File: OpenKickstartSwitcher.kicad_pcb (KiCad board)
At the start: 2 copper layers, 28.4 x 76.5 mm, 14 parts, among them J1 Conn_01x03, J2 Conn_01x04, J4 Conn_01x03, J98 LOGO, J99 OSHW_LOGO, U1 KS_SOCKET, U2 M27C800, U3 7400

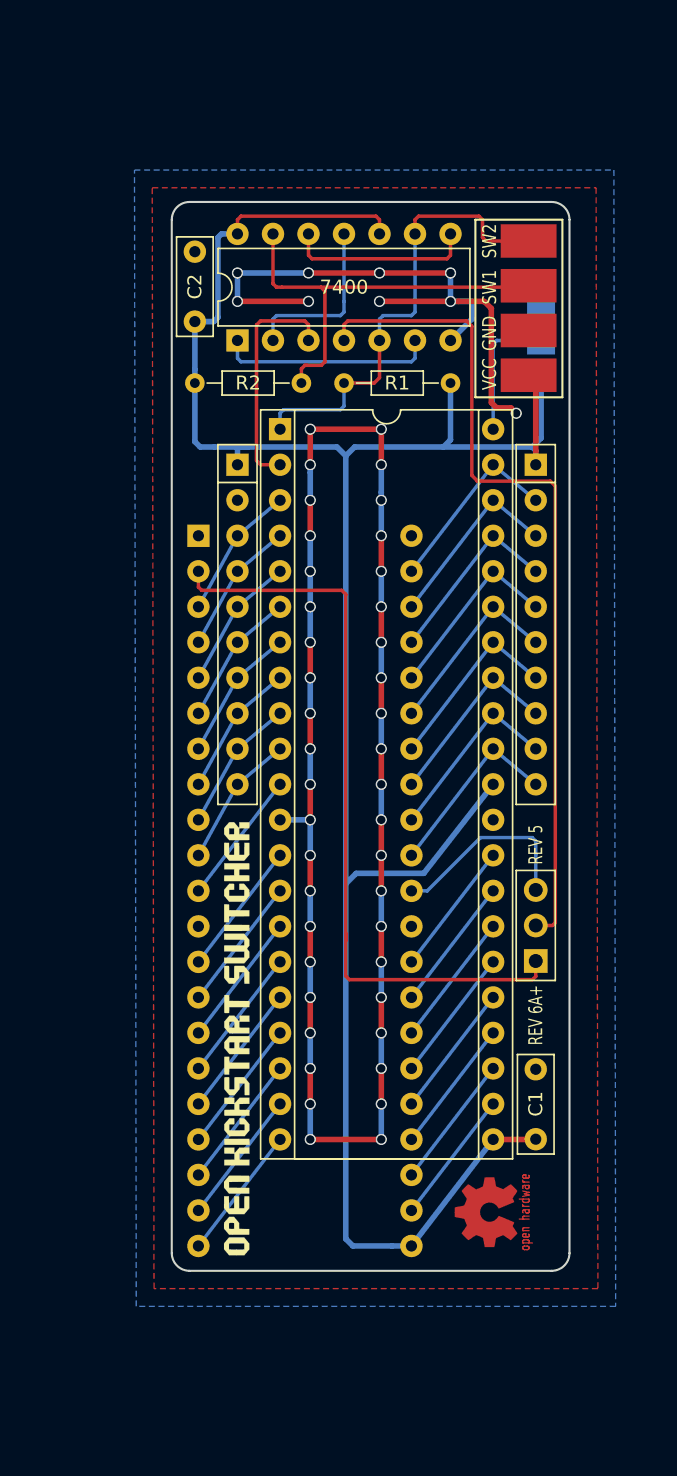
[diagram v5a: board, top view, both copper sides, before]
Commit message: Initial commit of CDTV version - NOT READY YET
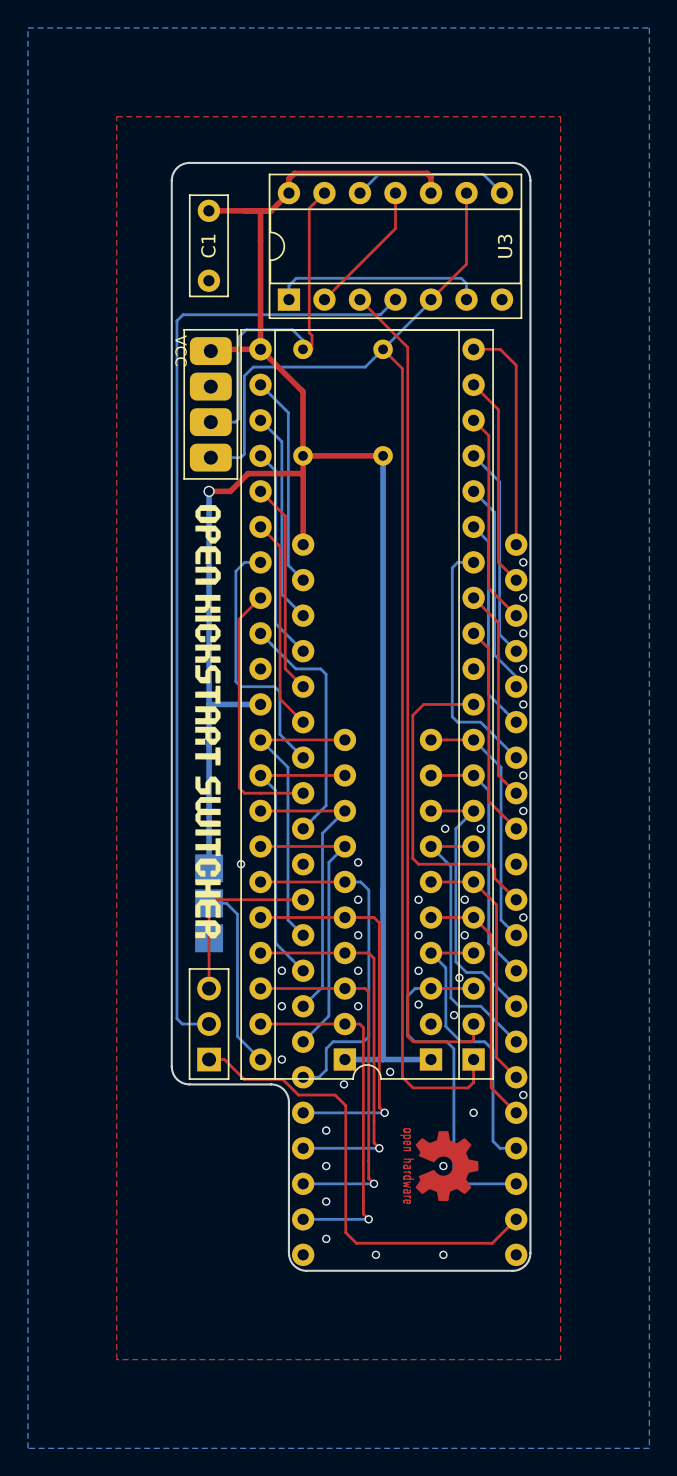
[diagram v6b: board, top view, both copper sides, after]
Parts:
- removed C2: 100n, Capacitors_THT:C_Disc_D7.0mm_W2.5mm_P5.00mm
- C1: footprint Capacitors_THT:C_Disc_D7.0mm_W2.5mm_P5.00mm -> Capacitor_THT:C_Disc_D7.0mm_W2.5mm_P5.00mm
- J2: footprint OpenKickstartSwitcher:LoosePads-4 -> OpenKickstartSwitcher:Solderable_PinHeader_1x04
- R1, R2: footprint Resistors_THT:R_Axial_DIN0204_L3.6mm_D1.6mm_P7.62mm_Horizontal -> Resistor_THT:R_Axial_DIN0204_L3.6mm_D1.6mm_P7.62mm_Horizontal; moved to B.Cu
- RN1, RN2: footprint Resistors_THT:R_Array_SIP10 -> Resistor_THT:R_Array_SIP10; moved to B.Cu
- U3: footprint Housings_DIP:DIP-14_W7.62mm -> Package_DIP:DIP-14_W7.62mm_Socket
- moved C1 70.4 mm to (146.3, 89.3), turned to 270 degrees
- moved U1 56.2 mm to (168.3, 164.0), turned to 180 degrees
- moved U2 47.2 mm to (165.2, 150.0), turned to 180 degrees
- moved J4 46.7 mm to (146.3, 138.8), turned to 270 degrees
- moved RN1 44.7 mm to (162.2, 150.0), turned to 90 degrees
- moved RN2 44.7 mm to (156.0, 150.0), turned to 90 degrees
- moved J2 25.1 mm to (146.4, 106.9), turned to 180 degrees
- moved J1 24.4 mm to (146.3, 150.0)
- moved J98 22.7 mm to (146.2, 125.9), turned to 270 degrees
- moved R2 9.32 mm to (153.0, 106.8), turned to 90 degrees
- moved R1 7.10 mm to (158.8, 106.8), turned to 90 degrees
- moved U3 4.70 mm to (152.0, 95.6)
- moved J99 4.33 mm to (163.3, 157.6), turned to 270 degrees
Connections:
- U1 pad 1: (no net) -> Net-(U1-Pad1)
- U1 pad 42: (no net) -> Net-(U1-Pad42)
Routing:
- net GND: track 160.3 -> 0.00 mm, vias 51 -> 38
- net /sw18: track 33.5 -> 92.4 mm
- net Net-(U2-Pad2): track 16.6 -> 60.2 mm
- net Net-(J1-Pad1): track 54.6 -> 33.4 mm
- net VCC: track 162.9 -> 144.1 mm, vias 0 -> 1
- net /a7: track 9.77 -> 25.1 mm
- net /a11: track 13.6 -> 28.2 mm, vias 0 -> 1
- net Net-(U1-Pad11): track 9.60 -> 23.9 mm
- net /a10: track 13.6 -> 27.5 mm, vias 0 -> 1
- net /a9: track 13.6 -> 26.8 mm, vias 0 -> 1
- net /a8: track 13.6 -> 26.0 mm, vias 0 -> 1
- net /a12: track 13.6 -> 25.3 mm
- net /a6: track 9.77 -> 21.2 mm
- net /a3: track 9.77 -> 20.4 mm
- net /a2: track 9.77 -> 20.0 mm
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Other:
- board size 28.4 x 76.5 mm -> 25.7 x 79.2 mm
- net class Default: clearance 0.25 -> 0.16; trace_width 0.25 -> 0.2
- net class Power: clearance 0.25 -> 0.16
- rule trace_clearance: 0.25 -> 0.16
- board text removed: "A19"
- board text removed: "GND"
- board text removed: "REV 5"
- board text removed: "REV 6A+"
- board text removed: "SW1"
- board text removed: "SW2"
- board text removed: "V2"
- board text removed: "github.com/SukkoPera/OpenKickstartSwitcher"

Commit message: Work in progress
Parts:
- moved C1 0.27 mm to (146.6, 89.3)
- moved J2 0.25 mm to (146.7, 106.9)
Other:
- board text added: "GND"
- board text added: "SW1"
- board text added: "SW2"
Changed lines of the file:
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@@
   (general
     (thickness 1.6)
-    (drawings 19)
+    (drawings 22)
     (tracks 347)
     (zones 0)
@@
   )
   (module OpenKickstartSwitcher:Solderable_PinHeader_1x04 (layer F.Cu)
-    (at 146.431 106.934 180)
+    (at 146.685 106.934 180)
     (descr "Through hole straight pin header, 1x04, 2.54mm pitch, single row")
     (tags "Through hole pin header THT 1x04 2.54mm single row")
@@
     (fp_line (start -1.27 8.89) (end -1.27 -0.635) (layer F.Fab) (width 0.1))
     (fp_line (start -1.27 -0.635) (end -0.635 -1.27) (layer F.Fab) (width 0.1))
-    (fp_line (start -1.905 9.144) (end 1.905 9.144) (layer F.SilkS) (width 0.12))
-    (fp_line (start -1.905 -1.524) (end -1.905 9.144) (layer F.SilkS) (width 0.12))
-    (fp_line (start 1.905 -1.524) (end 1.905 9.144) (layer F.SilkS) (width 0.12))
-    (fp_line (start -1.905 -1.524) (end 1.905 -1.524) (layer F.SilkS) (width 0.12))
     (fp_line (start -1.8 -1.8) (end -1.8 9.4) (layer F.CrtYd) (width 0.05))
     (fp_line (start -1.8 9.4) (end 1.8 9.4) (layer F.CrtYd) (width 0.05))
@@
       (effects (font (size 1 1) (thickness 0.15)))
     )
-    (pad 1 thru_hole roundrect (at 0 0 180) (size 3 2) (drill 1) (layers *.Cu *.Mask) (roundrect_rratio 0.25)
+    (pad 1 thru_hole roundrect (at 0 0 180) (size 2.8 2) (drill 1) (layers *.Cu *.Mask) (roundrect_rratio 0.25)
       (net 3 /sw18))
-    (pad 2 thru_hole roundrect (at 0 2.54 180) (size 3 2) (drill 1) (layers *.Cu *.Mask) (roundrect_rratio 0.25)
+    (pad 2 thru_hole roundrect (at 0 2.54 180) (size 2.8 2) (drill 1) (layers *.Cu *.Mask) (roundrect_rratio 0.25)
       (net 4 /sw17))
-    (pad 3 thru_hole roundrect (at 0 5.08 180) (size 3 2) (drill 1) (layers *.Cu *.Mask) (roundrect_rratio 0.25)
+    (pad 3 thru_hole roundrect (at 0 5.08 180) (size 2.8 2) (drill 1) (layers *.Cu *.Mask) (roundrect_rratio 0.25)
       (net 5 GND))
-    (pad 4 thru_hole roundrect (at 0 7.62 180) (size 3 2) (drill 1) (layers *.Cu *.Mask) (roundrect_rratio 0.25)
+    (pad 4 thru_hole roundrect (at 0 7.62 180) (size 2.8 2) (drill 1) (layers *.Cu *.Mask) (roundrect_rratio 0.25)
       (net 6 VCC))
     (model xxx${KISYS3DMOD}/Connector_PinHeader_2.54mm.3dshapes/PinHeader_1x04_P2.54mm_Vertical.wrl
@@
   )
   (module Capacitor_THT:C_Disc_D7.0mm_W2.5mm_P5.00mm (layer F.Cu)
-    (at 146.29237 89.281 270)
+    (at 146.558 89.281 270)
     (descr "C, Disc series, Radial, pin pitch=5.00mm, , diameter*width=7*2.5mm^2, Capacitor, http://cdn-reichelt.de/documents/datenblatt/B300/DS_KERKO_TC.pdf")
     (tags "C Disc series Radial pin pitch 5.00mm  diameter 7mm width 2.5mm Capacitor")
@@
     )
   )
-  (gr_text VCC (at 144.272 99.314 270) (layer F.SilkS)
+  (gr_text SW2 (at 144.399 106.934 270) (layer F.SilkS)
+    (effects (font (size 0.8 0.8) (thickness 0.15)))
+  )
+  (gr_text SW1 (at 144.399 104.394 270) (layer F.SilkS)
+    (effects (font (size 0.8 0.8) (thickness 0.15)))
+  )
+  (gr_text GND (at 144.399 101.854 270) (layer F.SilkS)
+    (effects (font (size 0.8 0.8) (thickness 0.15)))
+  )
+  (gr_text VCC (at 144.399 99.314 270) (layer F.SilkS)
     (effects (font (size 0.8 0.8) (thickness 0.15)))
   )
@@
   (gr_line (start 153.289 165.1) (end 168.021 165.1) (layer Edge.Cuts) (width 0.15))
   (gr_line (start 143.637 87.122) (end 143.637 150.495) (layer Edge.Cuts) (width 0.15))
-  (via (at 161.29 138.557) (size 0.6) (drill 0.4) (layers F.Cu B.Cu) (net 5))
-  (via (at 163.068 163.957) (size 0.6) (drill 0.4) (layers F.Cu B.Cu) (net 5))
   (segment (start 166.5605 163.1315) (end 168.275 161.417) (width 0.2) (layer F.Cu) (net 1))
   (segment (start 156.845 163.1315) (end 166.5605 163.1315) (width 0.2) (layer F.Cu) (net 1))
@@
   (segment (start 152.273 97.79) (end 152.970001 98.487001) (width 0.2) (layer B.Cu) (net 4))
   (segment (start 152.970001 98.487001) (end 153.67 99.187) (width 0.2) (layer B.Cu) (net 4))
+  (via (at 161.29 138.557) (size 0.6) (drill 0.4) (layers F.Cu B.Cu) (net 5))
+  (via (at 163.068 163.957) (size 0.6) (drill 0.4) (layers F.Cu B.Cu) (net 5))
   (via (at 163.195 133.477) (size 0.6) (drill 0.4) (layers F.Cu B.Cu) (net 5))
   (via (at 163.068 157.607) (size 0.6) (drill 0.4) (layers F.Cu B.Cu) (net 5))

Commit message: Work in progress
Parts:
- moved J1 0.63 mm to (146.9, 150.0)
- moved J98 0.25 mm to (146.4, 125.9)
- moved C1 0.13 mm to (146.7, 89.3)
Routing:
- net VCC: track 144.1 -> 142.6 mm
- net /a17: track 68.6 -> 67.5 mm
- net Net-(J1-Pad3): track 12.8 -> 12.1 mm
- net /sw18: track 92.4 -> 91.8 mm
- net GND: vias 38 -> 45
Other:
- board text added: "7400"
- board text added: "Licensed under CERN OHL v.1.2"
- board text added: "REV 5/6A+"
- board text added: "V1"
- board text added: "github.com/SukkoPera/ OpenKickstartSwitcher"
